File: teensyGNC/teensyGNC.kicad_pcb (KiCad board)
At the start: 4 copper layers, 58.8 x 149.5 mm, 45 parts, among them J1 5V_In_JST_XH, J10 TO_92_1_JST_PH, J11 TO_92_2_JST_PH, J12 TO_92_3_JST_PH, J13 TO_92_4_JST_PH, J14 Conn_Coaxial, J2 ESC_1_PWM_1x03, J3 ESC_2_PWM_1x03, J4 Servo_1_PWM_1x03, J5 Servo_2_PWM_1x03, J6 7V4_In_XT30M, J7 I2C_INA_BM_JST_GH, J8 MTF_01P_JST_SH, J9 LC29H_1x04, U1 LVL_Shift, U2 E28-2G4T20SX, U3 4754, U4 AP2112K-3.3, U5 DPS310, U6 Teensy4.1

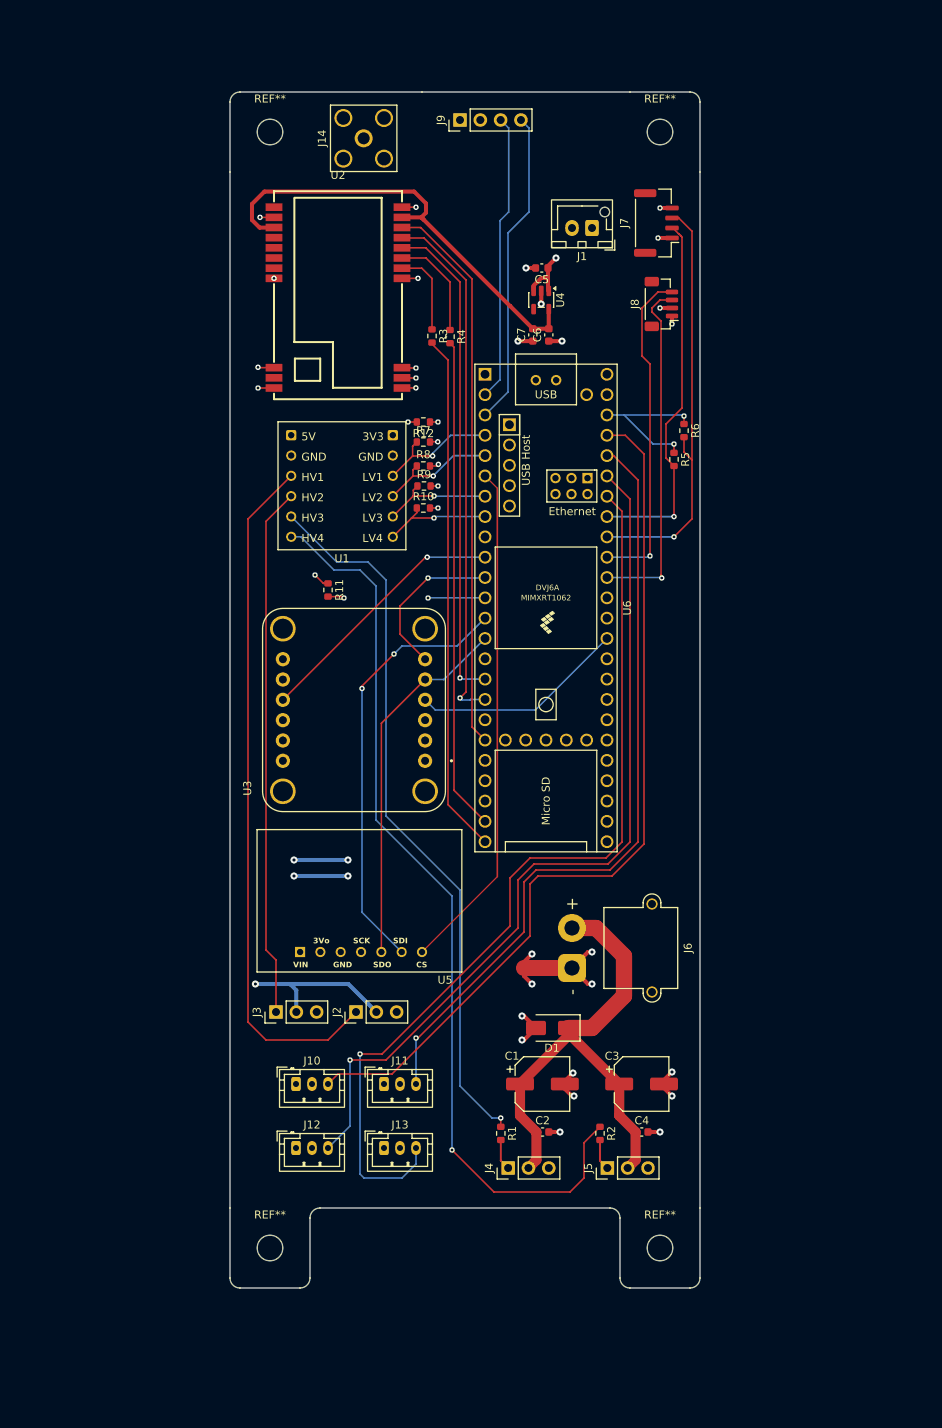
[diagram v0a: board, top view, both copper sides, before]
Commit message: Board width reduced
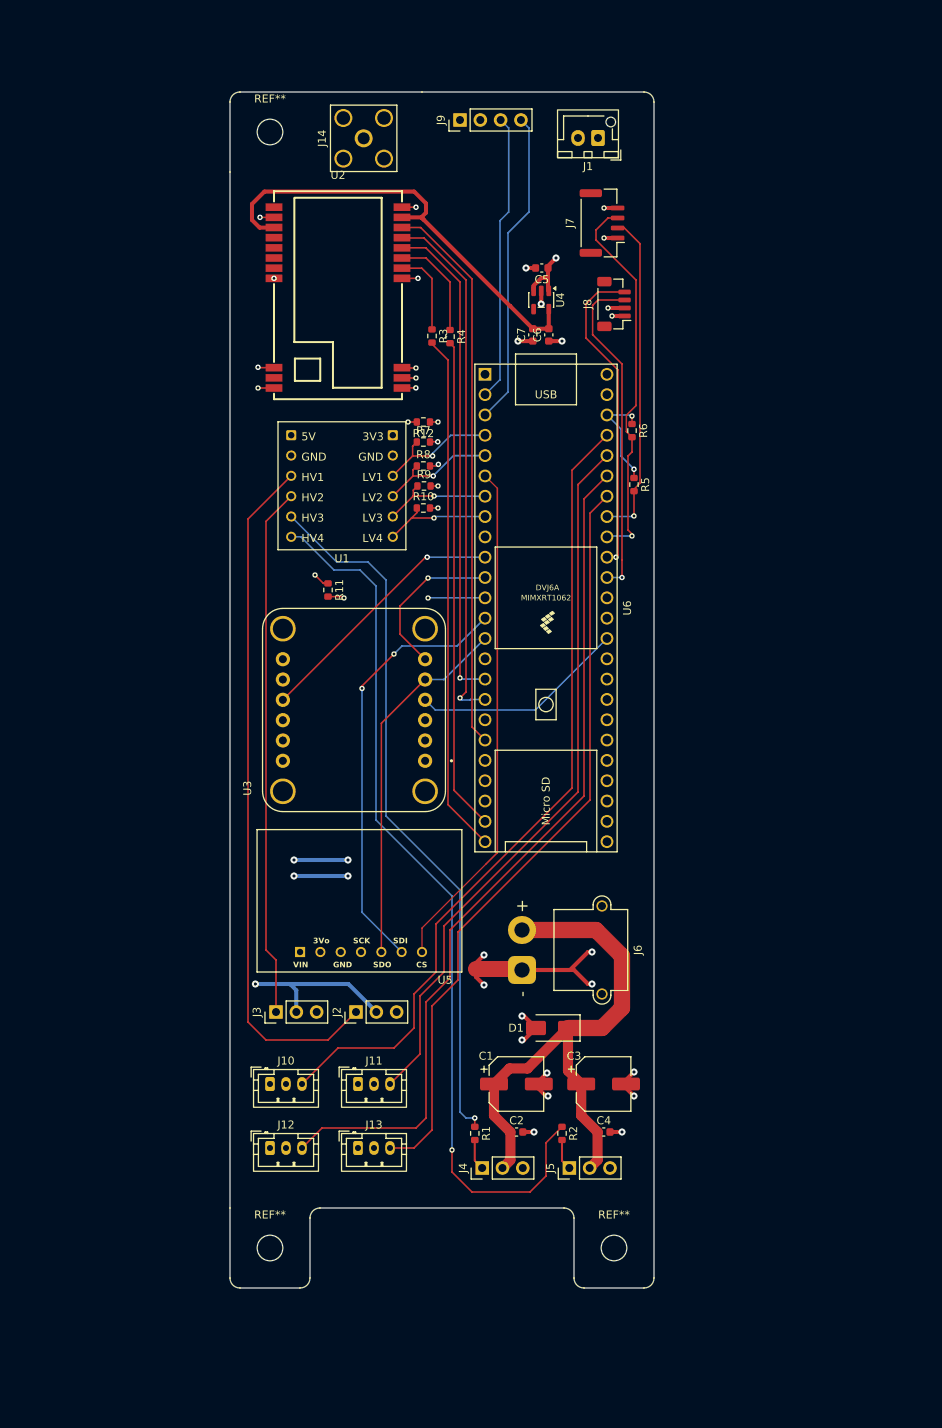
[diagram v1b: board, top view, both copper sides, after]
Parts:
- removed the REF** at (125.0, 31.8)
- moved J1 11.3 mm to (117.2, 32.5)
- moved J7 6.80 mm to (117.8, 43.1)
- moved R6 6.50 mm to (121.5, 69.1)
- moved J6 6.25 mm to (107.8, 136.5)
- moved NT1 6.00 mm to (104.0, 136.4)
- moved J8 5.92 mm to (119.2, 53.2)
- moved R5 5.91 mm to (121.8, 75.8)
- moved REF** 5.75 mm to (119.2, 171.2)
- moved C3 4.75 mm to (118.0, 150.8)
- moved C4 4.75 mm to (118.0, 156.8)
- moved J5 4.75 mm to (113.7, 161.2)
- moved R2 4.75 mm to (112.8, 156.9)
- moved C1 3.25 mm to (107.0, 150.8)
- moved C2 3.25 mm to (107.1, 156.8)
- moved J10 3.25 mm to (76.2, 150.8)
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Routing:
- net Net-(J13-Pin_3): track 116.2 -> 94.5 mm, vias 1 -> 0
- net +5V: track 211.6 -> 226.2 mm
- net PGND: track 22.1 -> 34.6 mm
- net Net-(J10-Pin_3): track 110.1 -> 101.0 mm
- net Net-(J11-Pin_3): track 97.7 -> 89.8 mm, vias 1 -> 0
- net +3V3: track 209.9 -> 202.4 mm
- net +7.4V: track 64.3 -> 71.5 mm
- net Net-(J7-Pin_3): track 54.0 -> 48.0 mm
- net Net-(J7-Pin_2): track 46.3 -> 41.4 mm
- net Net-(R2-Pad1): track 114.2 -> 110.9 mm
- net Net-(J8-Pin_3): track 44.0 -> 41.7 mm
- net Net-(J12-Pin_3): track 108.9 -> 106.7 mm, vias 1 -> 0
- net Net-(J8-Pin_4): track 41.4 -> 40.0 mm
- net Net-(R1-Pad1): track 90.1 -> 88.7 mm
- net GND: track 32.2 -> 33.0 mm
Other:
- board size 58.8 x 149.5 mm -> 53 x 149.5 mm

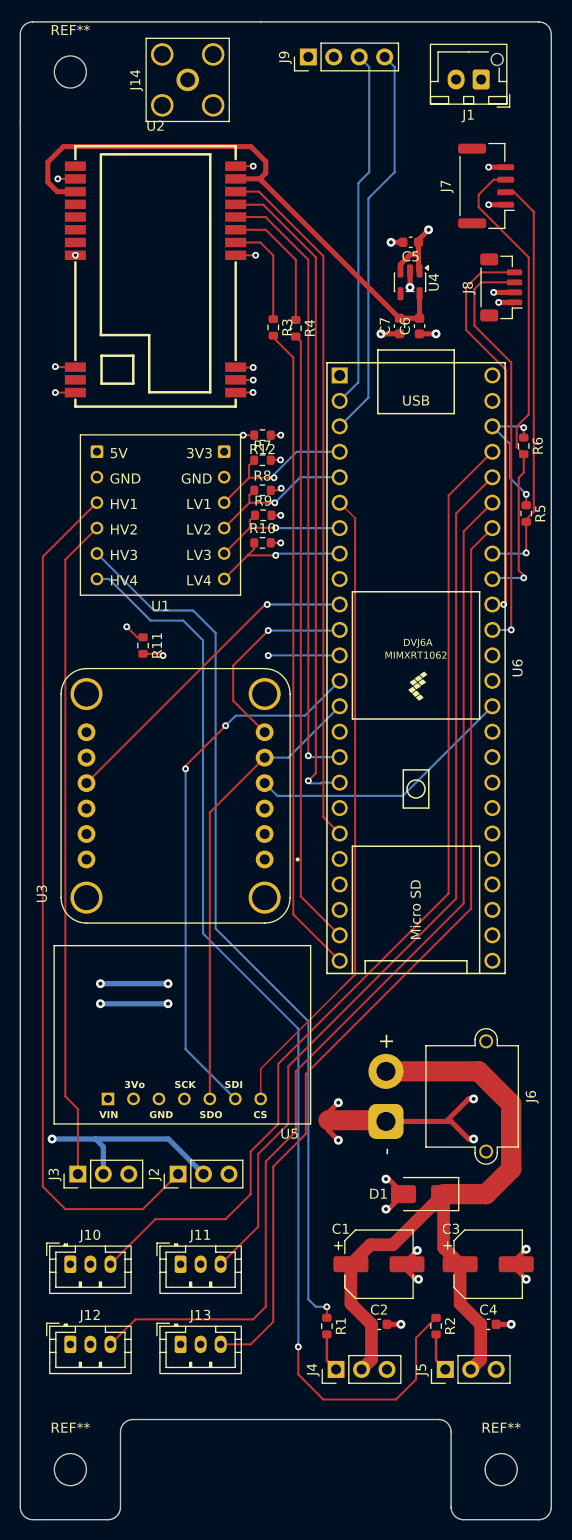
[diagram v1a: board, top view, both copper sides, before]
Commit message: Suggestions from Jack pt 1
- LVL shifter removed, both servo and escs tested to be OK with 3v3
- split plane removed, seems to be archaic method, and they haven't seen issues that require split ground planes to fix
- Trace for antennae added, need to add proper components for the pi matching network and trace sizes
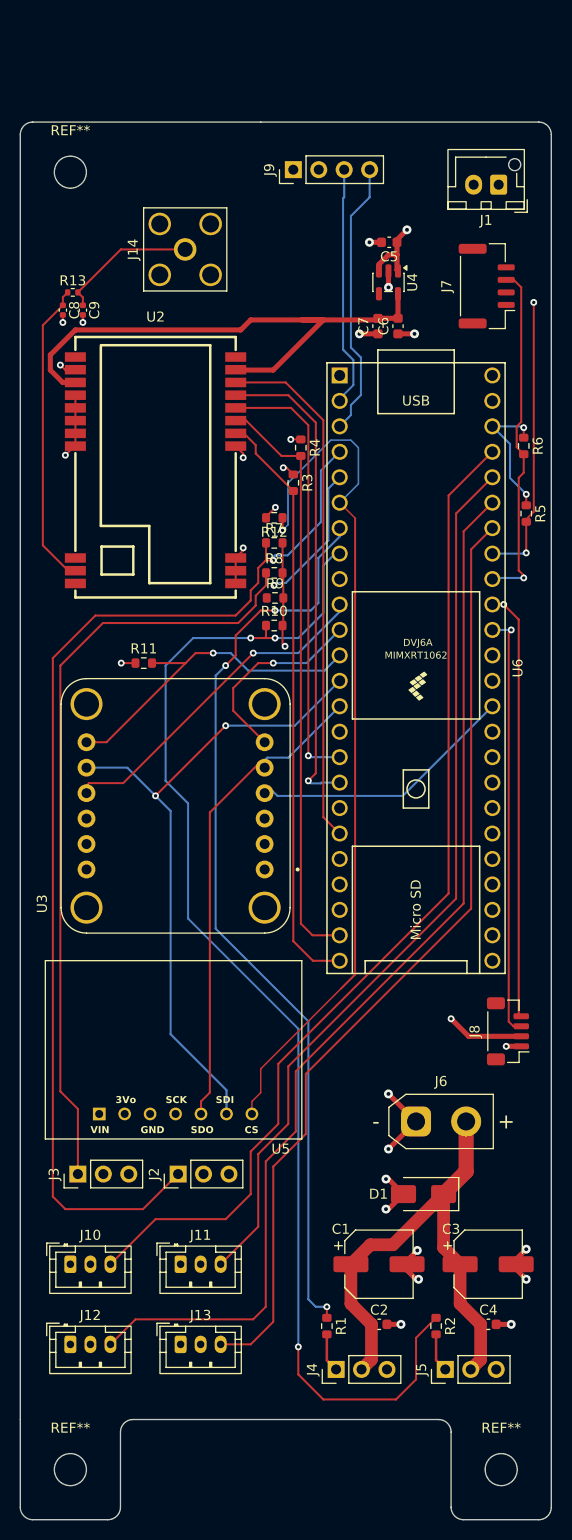
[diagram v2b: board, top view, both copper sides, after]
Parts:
- removed NT1: NetTie_2, NetTie:NetTie-2_SMD_Pad2.0mm
- removed U1: LVL_Shift, teensyGNC_footprints:MH_level_shifter
- added C8: C, Capacitor_SMD:C_0402_1005Metric, F.Cu at (75.5, 55.5)
- added C9: C, Capacitor_SMD:C_0402_1005Metric, F.Cu at (77.5, 55.5)
- added R13: 0Ω, Resistor_SMD:R_0402_1005Metric, F.Cu at (76.5, 53.8)
- J6: footprint Connector_AMASS:AMASS_XT30PW-M_1x02_P2.50mm_Horizontal -> Connector_AMASS:AMASS_XT30UPB-M_1x02_P5.0mm_Vertical
- moved J8 74.3 mm to (119.9, 127.5)
- moved U2 19.0 mm to (84.8, 71.5)
- moved J14 16.9 mm to (87.7, 49.5)
- moved R3 15.6 mm to (98.5, 72.8)
- moved R4 11.9 mm to (99.2, 69.2)
- moved J9 11.3 mm to (98.5, 41.5)
- moved J1 10.6 mm to (119.0, 43.0)
- moved J7 10.0 mm to (117.8, 53.1)
- moved REF** 10.0 mm to (76.2, 41.8)
- moved R10 8.33 mm to (96.6, 87.0)
- moved R12 8.33 mm to (96.6, 76.2)
- moved R7 8.33 mm to (96.6, 78.8)
- moved R8 8.33 mm to (96.6, 81.8)
- moved R9 8.33 mm to (96.7, 84.2)
- moved J6 3.00 mm to (110.8, 136.5), turned to 0 degrees
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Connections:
- C1 pad 2: PGND -> GND
- C2 pad 2: PGND -> GND
- C3 pad 2: PGND -> GND
- C4 pad 2: PGND -> GND
- D1 pad 2: PGND -> GND
- J14 pad 1: unconnected-(J14-In-Pad1) -> Net-(J14-In)
- J2 pad 2: +5V -> unconnected-(J2-Pin_2-Pad2)
- J3 pad 2: +5V -> unconnected-(J3-Pin_2-Pad2)
- J4 pad 3: PGND -> GND
- J5 pad 3: PGND -> GND
- J6 pad 1: PGND -> GND
- R1 pad 1: Net-(R1-Pad1) -> Net-(U6-5_IN2)
- R2 pad 1: Net-(R2-Pad1) -> Net-(U6-6_OUT1D)
- R7 pad 1: Net-(U6-2_OUT2) -> Net-(J2-Pin_1)
- R8 pad 1: Net-(U6-3_LRCLK2) -> Net-(J3-Pin_1)
- U2 pad 12: unconnected-(U2-ANT-Pad12) -> Net-(U2-ANT)
- U2 pad 4: unconnected-(U2-NC-Pad4) -> GND
- U2 pad 5: unconnected-(U2-NC-Pad5) -> GND
- U2 pad 6: unconnected-(U2-NC-Pad6) -> GND
- U2 pad 7: unconnected-(U2-NC-Pad7) -> GND
- U6 pad 4: Net-(U6-2_OUT2) -> Net-(J2-Pin_1)
- U6 pad 5: Net-(U6-3_LRCLK2) -> Net-(J3-Pin_1)
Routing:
- net +3V3: track 202.4 -> 18.6 mm, vias 8 -> 4
- net Net-(R2-Pad1): track 110.9 -> 0.00 mm, vias 1 -> 0
- net Net-(U6-6_OUT1D): track 14.4 -> 123.4 mm, vias 1 -> 3
- net +5V: track 226.2 -> 125.8 mm, vias 4 -> 2
- net Net-(R1-Pad1): track 88.7 -> 0.00 mm, vias 1 -> 0
- net Net-(U6-5_IN2): track 14.1 -> 92.2 mm, vias 1 -> 3
- net PGND: track 34.6 -> 0.00 mm, vias 10 -> 0
- net Net-(U2-ANT): track 0.00 -> 30.6 mm
- net GND: track 33.0 -> 58.7 mm, vias 21 -> 24
- net Net-(J2-Pin_1): track 86.4 -> 111.8 mm, vias 0 -> 1
- net Net-(J3-Pin_1): track 66.3 -> 91.3 mm, vias 0 -> 1
- net +7.4V: track 71.5 -> 51.5 mm
- net Net-(U2-TXD): track 66.6 -> 48.5 mm
- net Net-(U2-AUX): track 70.3 -> 52.2 mm
- net Net-(U2-RXD): track 61.7 -> 44.2 mm
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- added copper zone on In2.Cu, net +3V3
- removed copper zone on In1.Cu, net PGND
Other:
- board size 53 x 149.5 mm -> 53 x 139.5 mm

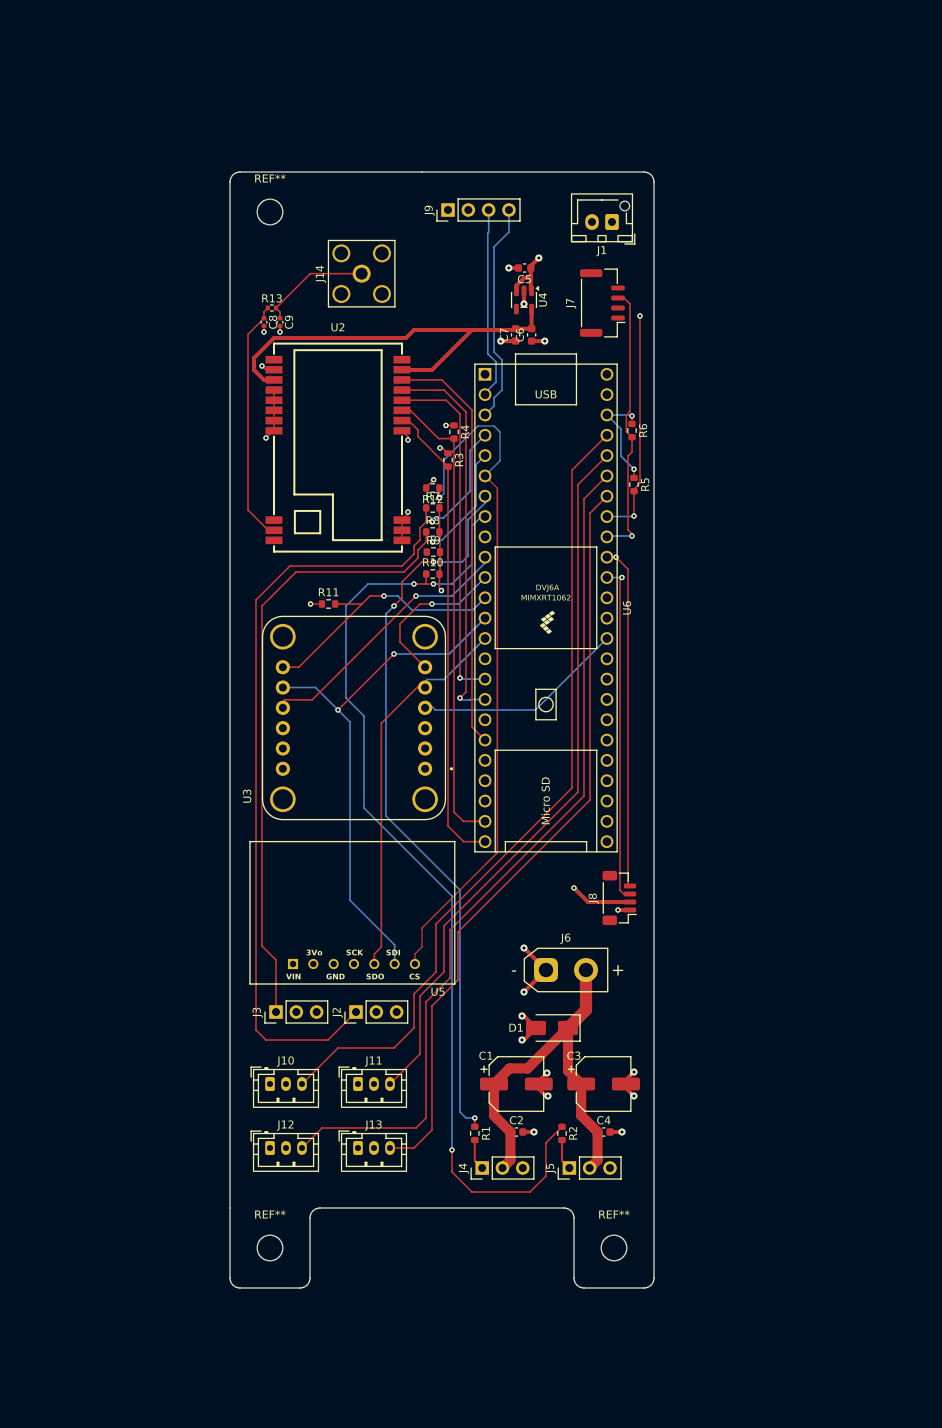
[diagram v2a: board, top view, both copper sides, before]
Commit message: Suggestions from Jack part 2 + some other changes
- Ground pours on signal planes
- Capacitors changed to flatter versions
- Connector movements for teensy usb clearance
- Silkscreen labels
- Ran DRC; no errors just text warnings
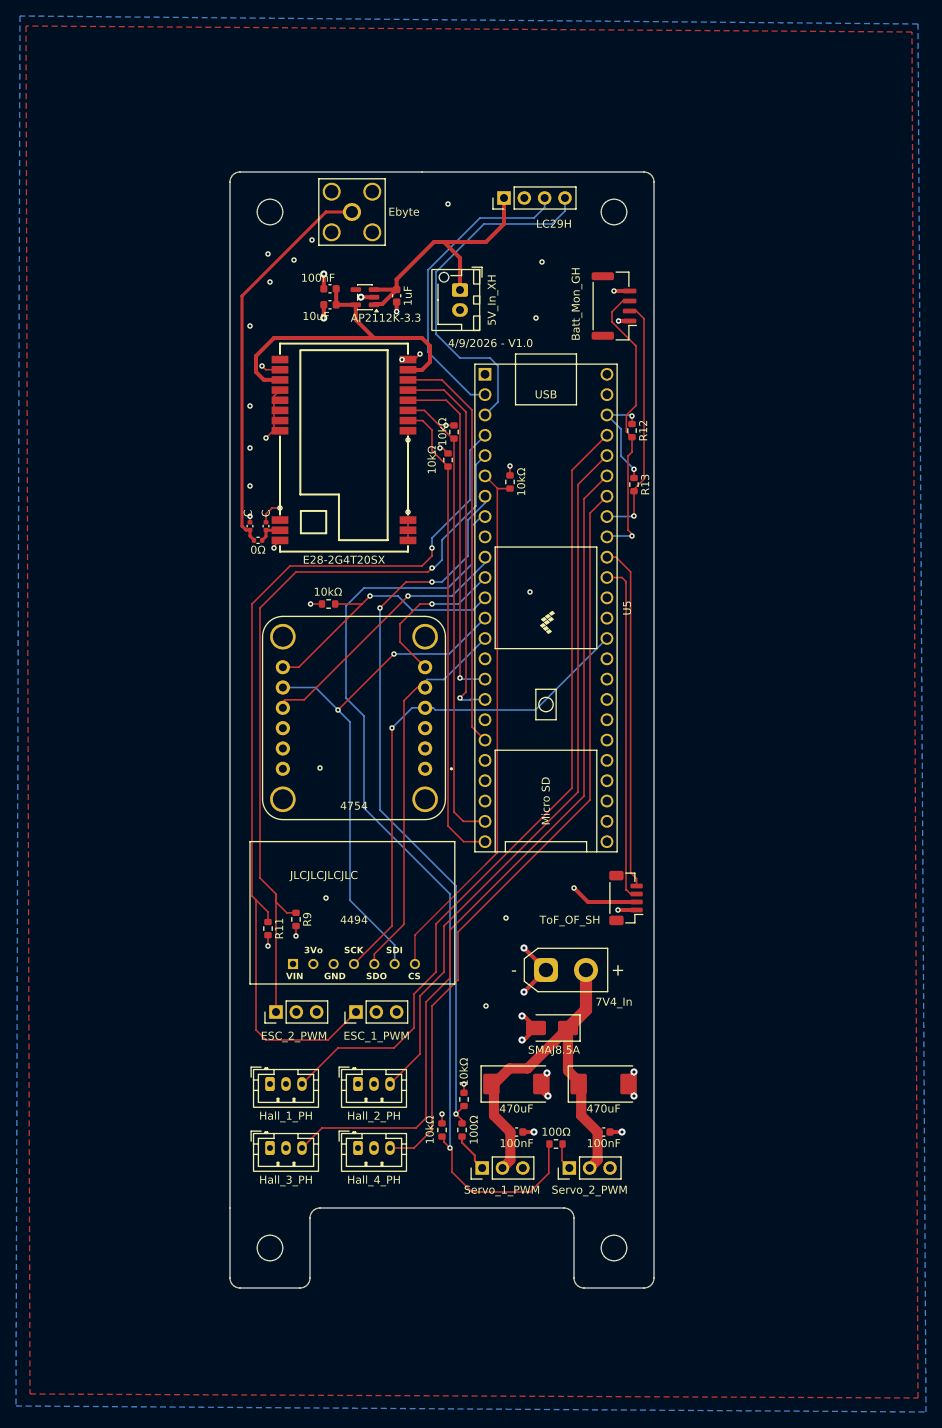
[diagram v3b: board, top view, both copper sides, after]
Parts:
- added REF**: MountingHole_3.2mm_M3, MountingHole:MountingHole_3.2mm_M3, F.Cu at (119.2, 41.8)
- C1, C3: footprint Capacitor_SMD:CP_Elec_6.3x5.4 -> Capacitor_Tantalum_SMD:CP_EIA-7343-43_Kemet-X
- J1: renamed from J2; value ESC_1_PWM_1x03 -> ESC_1_PWM
- J10: renamed from J8; value MTF_01P_JST_SH -> ToF_OF_SH
- J11: renamed from J10; value TO_92_1_JST_PH -> Hall_1_PH
- J12: renamed from J11; value TO_92_2_JST_PH -> Hall_2_PH
- J13: renamed from J12; value TO_92_3_JST_PH -> Hall_3_PH
- J14: renamed from J13; value TO_92_4_JST_PH -> Hall_4_PH
- J2: renamed from J1; value 5V_In_JST_XH -> 5V_In_XH
- J3: value ESC_2_PWM_1x03 -> ESC_2_PWM
- J4: value Servo_1_PWM_1x03 -> Servo_1_PWM
- J5: value Servo_2_PWM_1x03 -> Servo_2_PWM
- J6: value 7V4_In_XT30M -> 7V4_In
- J7: renamed from J14; value Conn_Coaxial -> Ebyte
- J8: renamed from J9; value LC29H_1x04 -> LC29H
- J9: renamed from J7; value I2C_INA_BM_JST_GH -> Batt_Mon_GH
- U4: renamed from U5; value DPS310 -> 4494
- moved R6 69.5 mm to (97.8, 156.5), turned to 90 degrees
- moved R7 68.5 mm to (100.5, 152.7), turned to 90 degrees
- moved R11 56.5 mm to (76.0, 131.3), turned to -90 degrees
- moved R9 51.4 mm to (79.5, 130.2), turned to -90 degrees
- moved R4 29.1 mm to (74.8, 82.8), turned to 180 degrees
- moved C6 25.8 mm to (73.8, 81.0), turned to 90 degrees
- moved C5 25.5 mm to (75.8, 81.0), turned to 90 degrees
- moved C8 25.5 mm to (83.8, 53.4), turned to 0 degrees
- moved C9 23.9 mm to (83.8, 51.4), turned to 0 degrees
- moved J2 20.8 mm to (100.0, 51.5), turned to -90 degrees
- moved U3 19.9 mm to (88.1, 52.4), turned to 180 degrees
- moved C7 16.4 mm to (92.1, 52.2), turned to -90 degrees
- moved R5 9.68 mm to (106.2, 75.5), turned to 90 degrees
- moved J7 7.80 mm to (86.5, 41.8)
- moved J8 7.16 mm to (105.5, 40.0)
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- renumbered C8 to C5, C9 to C6, C5 to C7, C6 to C8, C7 to C9, R3 to R10, R7 to R11, R6 to R12, R5 to R13, R11 to R3, R13 to R4, R12 to R5, R10 to R6, R9 to R7, R4 to R8, R8 to R9, U2 to U1, U3 to U2, U4 to U3, U6 to U5
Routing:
- net Net-(J7-In): track 14.0 -> 49.6 mm
- net Net-(U1-ANT): track 30.6 -> 3.25 mm
- net /SPI.CS_DPS: track 87.5 -> 67.5 mm, vias 1 -> 0
- net +5V: track 125.8 -> 143.1 mm
- net Net-(J8-Pin_4): track 27.7 -> 44.9 mm
- net Net-(J8-Pin_3): track 24.1 -> 38.6 mm
- net Net-(U1-M2): track 56.2 -> 43.5 mm
- net /SPI.SCL: track 68.1 -> 63.2 mm, vias 0 -> 1
- net Net-(J3-Pin_1): track 91.3 -> 95.9 mm
- net GND: track 58.7 -> 63.2 mm, vias 24 -> 47
- net Net-(U5-6_OUT1D): track 123.4 -> 120.7 mm, vias 3 -> 1
- net Net-(J1-Pin_1): track 111.8 -> 114.1 mm
- net Net-(J9-Pin_2): track 28.7 -> 30.8 mm, vias 2 -> 1
- net Net-(J9-Pin_3): track 34.9 -> 36.4 mm
- net /SPI.RST: track 35.3 -> 33.9 mm
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- added copper zone on B.Cu, net GND
- added copper zone on F.Cu, net GND
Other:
- board text added: "4/9/2026 - V1.0"
- board text added: "JLCJLCJLCJLC"
